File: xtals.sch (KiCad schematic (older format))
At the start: 6 parts

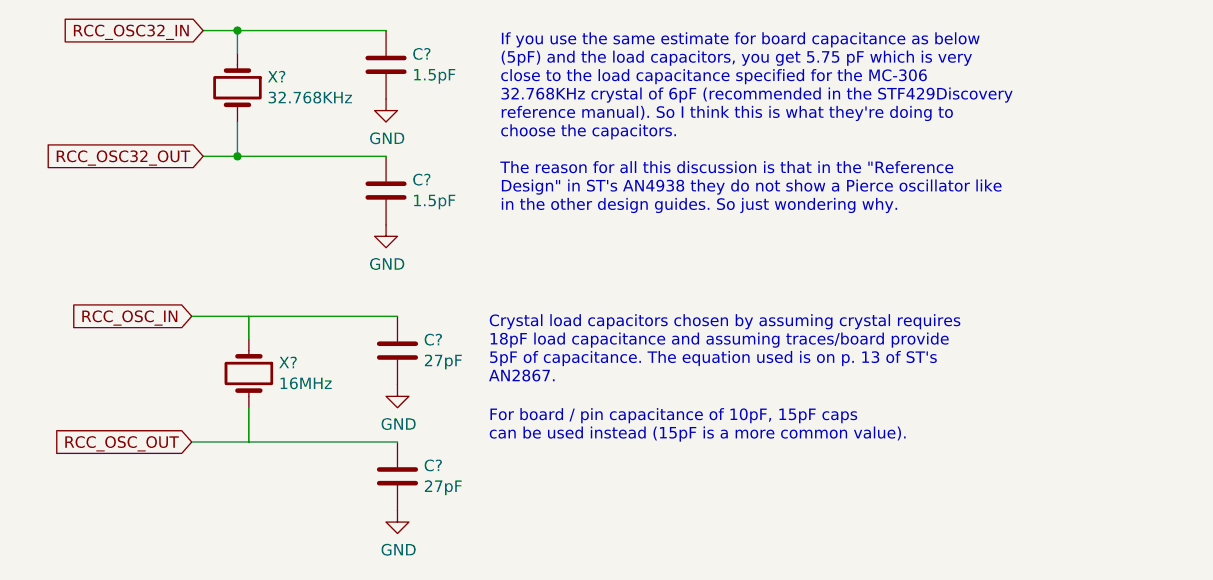
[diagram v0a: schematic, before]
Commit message: First proposed pin layout of SODIMM connector
Will need to add GPIO / ADC pins as needed, but let's wait to see if we don't
need to use more pins.

Double-checked and fixed CODEC and MCU's power supply.
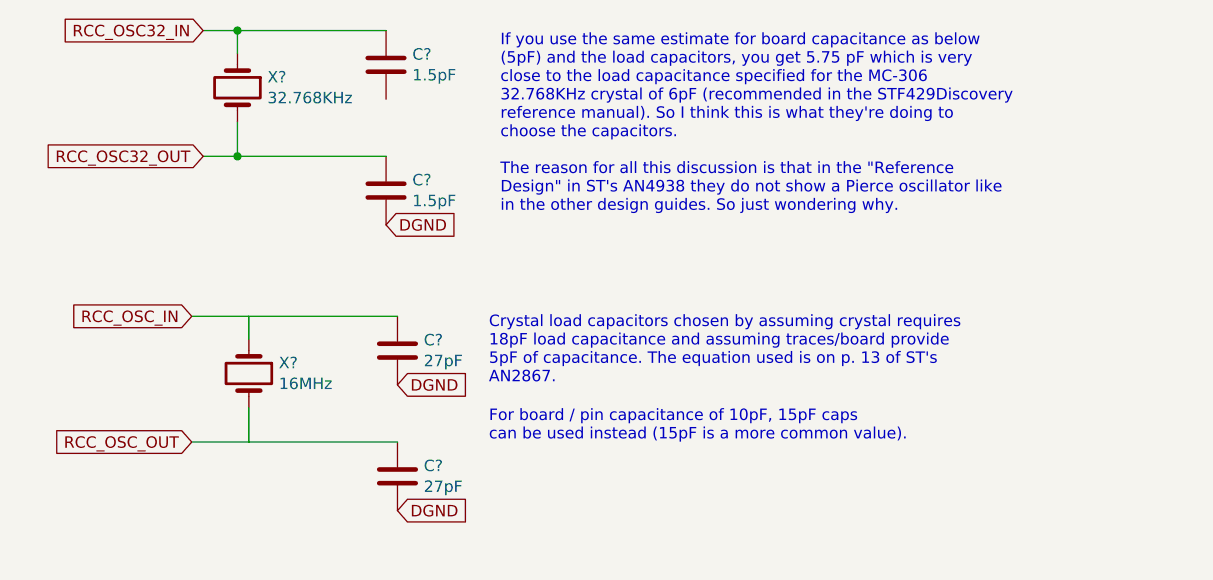
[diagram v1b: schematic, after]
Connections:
- net GND renamed DGND
- net DGND: no longer C?.2
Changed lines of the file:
@@
 $Descr A4 11693 8268
 encoding utf-8
-Sheet 4 12
+Sheet 4 13
 Title ""
 Date ""
@@
 Connection ~ 2600 1400
 $Comp
-L power:GND #PWR?
-U 1 1 5CF5FA29
-P 3250 1150
-F 0 "#PWR?" H 3250 900 50  0001 C CNN
-F 1 "GND" H 3255 977 50  0000 C CNN
-F 2 "" H 3250 1150 50  0001 C CNN
-F 3 "" H 3250 1150 50  0001 C CNN
-	1    3250 1150
-	1    0    0    -1
-$EndComp
-$Comp
-L power:GND #PWR?
-U 1 1 5CF5FA57
-P 3250 1700
-F 0 "#PWR?" H 3250 1450 50  0001 C CNN
-F 1 "GND" H 3255 1527 50  0000 C CNN
-F 2 "" H 3250 1700 50  0001 C CNN
-F 3 "" H 3250 1700 50  0001 C CNN
-	1    3250 1700
-	1    0    0    -1
-$EndComp
-$Comp
 L Device:C C?
 U 1 1 5CF5FC4F
@@
 Wire Wire Line
 	2650 2650 3300 2650
-$Comp
-L power:GND #PWR?
-U 1 1 5CF5FC5F
-P 3300 2400
-F 0 "#PWR?" H 3300 2150 50  0001 C CNN
-F 1 "GND" H 3305 2227 50  0000 C CNN
-F 2 "" H 3300 2400 50  0001 C CNN
-F 3 "" H 3300 2400 50  0001 C CNN
-	1    3300 2400
-	1    0    0    -1
-$EndComp
-$Comp
-L power:GND #PWR?
-U 1 1 5CF5FC65
-P 3300 2950
-F 0 "#PWR?" H 3300 2700 50  0001 C CNN
-F 1 "GND" H 3305 2777 50  0000 C CNN
-F 2 "" H 3300 2950 50  0001 C CNN
-F 3 "" H 3300 2950 50  0001 C CNN
-	1    3300 2950
-	1    0    0    -1
-$EndComp
 Text Notes 3700 2400 0    50   ~ 0
 Crystal load capacitors chosen by assuming crystal requires \n18pF load capacitance and assuming traces/board provide \n5pF of capacitance. The equation used is on p. 13 of ST's \nAN2867.
@@
 Text Notes 3700 2650 0    50   ~ 0
 For board / pin capacitance of 10pF, 15pF caps\ncan be used instead (15pF is a more common value).
+Text GLabel 3250 1700 2    50   Input ~ 0
+DGND
+Text GLabel 3300 2400 2    50   Input ~ 0
+DGND
+Text GLabel 3300 2950 2    50   Input ~ 0
+DGND
 $EndSCHEMATC
